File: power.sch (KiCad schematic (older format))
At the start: 8 parts

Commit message: Added some footprints. Basic board outline.
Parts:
- C1: renamed from C?; footprint (none) -> Capacitor_THT:CP_Radial_D5.0mm_P2.00mm; symbol Device:CP -> Device:C
- C2: renamed from C?; footprint (none) -> Capacitor_THT:C_Disc_D5.0mm_W2.5mm_P2.50mm
- F1: renamed from F?; footprint (none) -> Diode_THT:D_DO-15_P10.16mm_Horizontal
- J9: renamed from J?; footprint (none) -> Connector_USB:USB_B_OST_USB-B1HSxx_Horizontal
- R1: renamed from R?; footprint (none) -> Resistor_THT:R_Axial_DIN0411_L9.9mm_D3.6mm_P12.70mm_Horizontal
- SW1: renamed from SW?; footprint (none) -> Button_Switch_THT:SW_Push_1P2T_Vertical_E-Switch_800UDP8P1A1M6
- SW2: renamed from SW?; footprint (none) -> Button_Switch_THT:SW_PUSH-12mm
- gave numbers to parts that had none: 1
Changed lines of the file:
@@
 $Descr A4 11693 8268
 encoding utf-8
-Sheet 6 11
+Sheet 5 11
 Title "Neotron 32K"
 Date "2019-12-08"
@@
 ~RESET
 $Comp
-L Connector:USB_B J?
+L Connector:USB_B J9
 U 1 1 5DFCA02C
 P 3200 2400
-F 0 "J?" H 3200 2850 50  0000 C CNN
+F 0 "J9" H 3200 2850 50  0000 C CNN
 F 1 "USB_B" H 3200 2750 50  0000 C CNN
-F 2 "" H 3350 2350 50  0001 C CNN
+F 2 "Connector_USB:USB_B_OST_USB-B1HSxx_Horizontal" H 3350 2350 50  0001 C CNN
 F 3 " ~" H 3350 2350 50  0001 C CNN
 	1    3200 2400
@@
 $EndComp
 $Comp
-L power:+5V #PWR?
+L power:+5V #PWR011
 U 1 1 5DFCBF4D
 P 6300 2050
-F 0 "#PWR?" H 6300 1900 50  0001 C CNN
+F 0 "#PWR011" H 6300 1900 50  0001 C CNN
 F 1 "+5V" H 6315 2223 50  0000 C CNN
 F 2 "" H 6300 2050 50  0001 C CNN
@@
 NoConn ~ 3500 2500
 $Comp
-L Device:CP C?
+L Device:C C1
 U 1 1 5DFCD9F0
 P 5700 2300
-F 0 "C?" H 5818 2346 50  0000 L CNN
+F 0 "C1" H 5818 2346 50  0000 L CNN
 F 1 "47u" H 5818 2255 50  0000 L CNN
-F 2 "" H 5738 2150 50  0001 C CNN
+F 2 "Capacitor_THT:CP_Radial_D5.0mm_P2.00mm" H 5738 2150 50  0001 C CNN
 F 3 "~" H 5700 2300 50  0001 C CNN
 	1    5700 2300
@@
 $EndComp
 $Comp
-L Device:C C?
+L Device:C C2
 U 1 1 5DFCDDA8
 P 6100 2300
-F 0 "C?" H 6215 2346 50  0000 L CNN
+F 0 "C2" H 6215 2346 50  0000 L CNN
 F 1 "1u" H 6215 2255 50  0000 L CNN
-F 2 "" H 6138 2150 50  0001 C CNN
+F 2 "Capacitor_THT:C_Disc_D5.0mm_W2.5mm_P2.50mm" H 6138 2150 50  0001 C CNN
 F 3 "~" H 6100 2300 50  0001 C CNN
 	1    6100 2300
@@
 $EndComp
 $Comp
-L Device:Polyfuse F?
+L Device:Polyfuse F1
 U 1 1 5DFCE179
 P 4850 2100
-F 0 "F?" V 4625 2100 50  0000 C CNN
+F 0 "F1" V 4625 2100 50  0000 C CNN
 F 1 "250mA PTC" V 4716 2100 50  0000 C CNN
-F 2 "" H 4900 1900 50  0001 L CNN
+F 2 "Diode_THT:D_DO-15_P10.16mm_Horizontal" H 4900 1900 50  0001 L CNN
 F 3 "https://www.littelfuse.com/~/media/electronics/product_specifications/resettable_ptcs/littelfuse_ptc_rxef025_product_specification.pdf.pdf" H 4850 2100 50  0001 C CNN
 F 4 "RXEF025HF-ND" V 4850 2100 50  0001 C CNN "Digikey"
@@
 $EndComp
 $Comp
-L Device:D_TVS D?
+L Device:D_TVS D1
 U 1 1 5DFD0F1E
 P 5200 2300
-F 0 "D?" V 5154 2379 50  0000 L CNN
+F 0 "D1" V 5154 2379 50  0000 L CNN
 F 1 "SA5.0A" V 5245 2379 50  0000 L CNN
 F 2 "Diode_THT:D_DO-15_P12.70mm_Horizontal" H 5200 2300 50  0001 C CNN
@@
 Connection ~ 5700 2500
 $Comp
-L power:GND #PWR?
+L power:GND #PWR012
 U 1 1 5DFD4FCF
 P 6300 2550
-F 0 "#PWR?" H 6300 2300 50  0001 C CNN
+F 0 "#PWR012" H 6300 2300 50  0001 C CNN
 F 1 "GND" H 6305 2377 50  0000 C CNN
 F 2 "" H 6300 2550 50  0001 C CNN
@@
 Connection ~ 6100 2500
 $Comp
-L Switch:SW_Push SW?
+L Switch:SW_Push SW2
 U 1 1 5DFD5E14
 P 7400 2500
-F 0 "SW?" H 7400 2785 50  0000 C CNN
+F 0 "SW2" H 7400 2785 50  0000 C CNN
 F 1 "SW_Push" H 7400 2694 50  0000 C CNN
-F 2 "" H 7400 2700 50  0001 C CNN
+F 2 "Button_Switch_THT:SW_PUSH-12mm" H 7400 2700 50  0001 C CNN
 F 3 "~" H 7400 2700 50  0001 C CNN
 	1    7400 2500
@@
 $EndComp
 $Comp
-L Switch:SW_SPDT SW?
+L Switch:SW_SPDT SW1
 U 1 1 5DFD696E
 P 4000 2200
-F 0 "SW?" H 4000 2485 50  0000 C CNN
+F 0 "SW1" H 4000 2485 50  0000 C CNN
 F 1 "SW_SPDT" H 4000 2394 50  0000 C CNN
-F 2 "" H 4000 2200 50  0001 C CNN
+F 2 "Button_Switch_THT:SW_Push_1P2T_Vertical_E-Switch_800UDP8P1A1M6" H 4000 2200 50  0001 C CNN
 F 3 "~" H 4000 2200 50  0001 C CNN
 	1    4000 2200
@@
 	3200 2800 3200 2850
 $Comp
-L Device:R R?
+L Device:R R1
 U 1 1 5DFD98A8
 P 3100 3000
-F 0 "R?" H 3030 2954 50  0000 R CNN
+F 0 "R1" H 3030 2954 50  0000 R CNN
 F 1 "DNF" H 3030 3045 50  0000 R CNN
-F 2 "" V 3030 3000 50  0001 C CNN
+F 2 "Resistor_THT:R_Axial_DIN0411_L9.9mm_D3.6mm_P12.70mm_Horizontal" V 3030 3000 50  0001 C CNN
 F 3 "~" H 3100 3000 50  0001 C CNN
 	1    3100 3000
@@
 $EndComp
 $Comp
-L power:GND #PWR?
+L power:GND #PWR010
 U 1 1 5DFDADE6
 P 3100 3200
-F 0 "#PWR?" H 3100 2950 50  0001 C CNN
+F 0 "#PWR010" H 3100 2950 50  0001 C CNN
 F 1 "GND" H 3105 3027 50  0000 C CNN
 F 2 "" H 3100 3200 50  0001 C CNN
@@
 	4200 2100 4700 2100
 $Comp
-L power:GND #PWR?
+L power:GND #PWR013
 U 1 1 5DFDC03E
 P 7150 2600
-F 0 "#PWR?" H 7150 2350 50  0001 C CNN
+F 0 "#PWR013" H 7150 2350 50  0001 C CNN
 F 1 "GND" H 7155 2427 50  0000 C CNN
 F 2 "" H 7150 2600 50  0001 C CNN

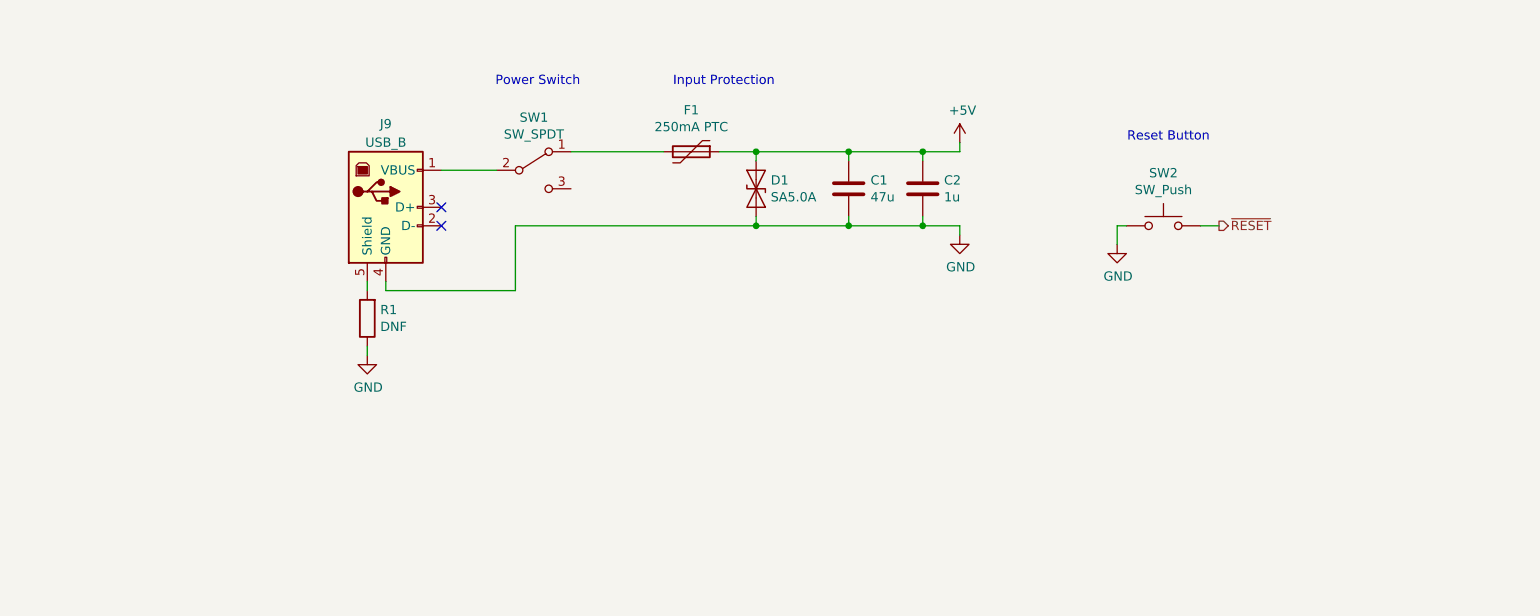
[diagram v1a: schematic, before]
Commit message: Completed Power, SD, MIDI, Parallel and Joystick sheets.
Switch to sheet based 100x part numbering.
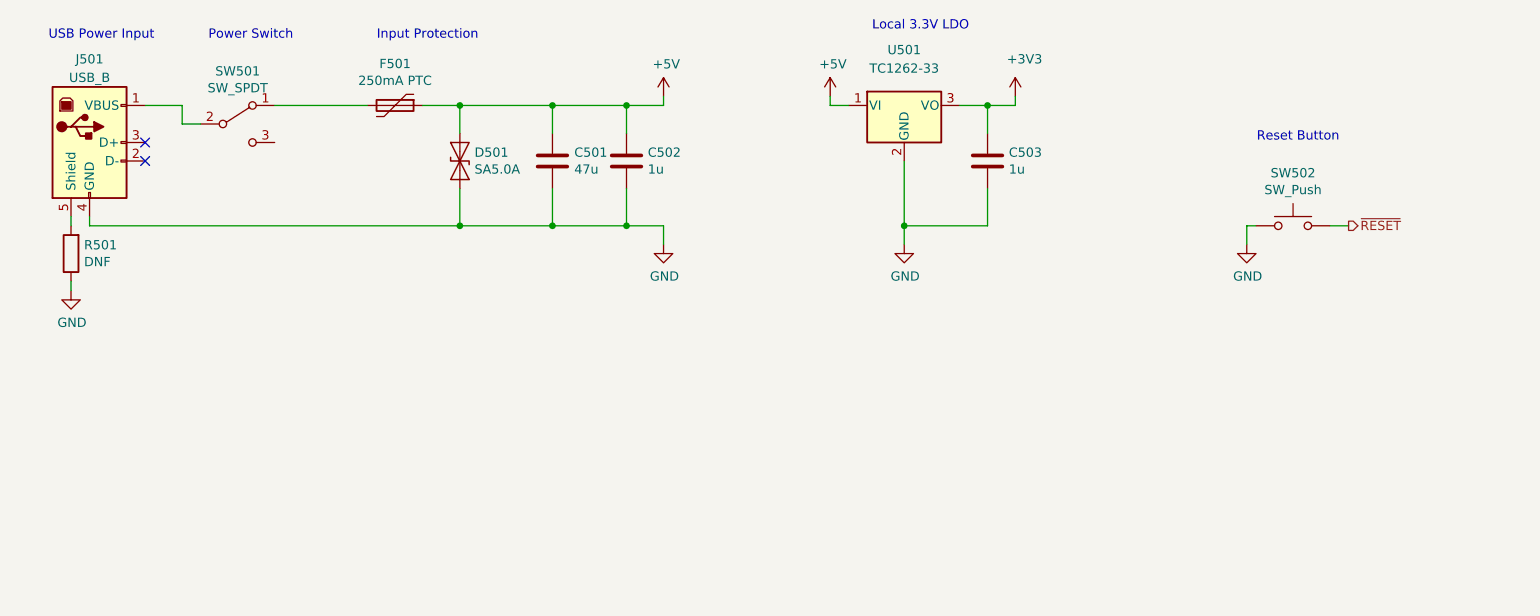
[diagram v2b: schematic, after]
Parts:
- added C503: 1u, Capacitor_THT:C_Disc_D5.0mm_W2.5mm_P2.50mm, symbol Device:C
- added U501: TC1262-33, symbol Regulator_Linear:TC1262-33
- renumbered C1 to C501, C2 to C502, D1 to D501, F1 to F501, J9 to J501, R1 to R501, SW1 to SW501, SW2 to SW502
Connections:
- net +5V: now also U501.1 (VI)
- net GND: now also C503.2, U501.2 (GND)
- new net +3V3: C503.1, U501.3 (VO)
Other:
- note added: "Local 3.3V LDO"
- note added: "USB Power Input"
- moved on the sheet: C501, C502, D501, F501, J501, R501, SW501, SW502

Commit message: Schematic capture draft complete.
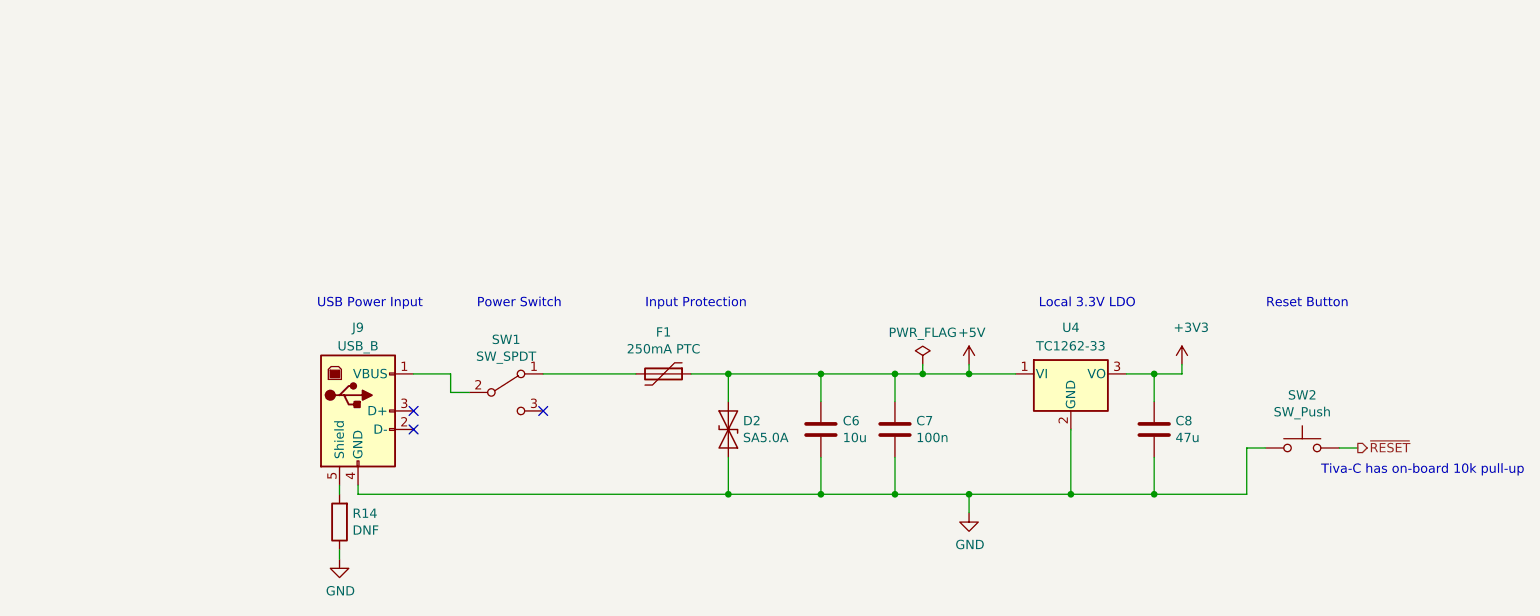
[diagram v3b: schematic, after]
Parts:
- C6: renamed from C501; value 47u -> 10u; footprint Capacitor_THT:CP_Radial_D5.0mm_P2.00mm -> Capacitor_THT:C_Disc_D3.0mm_W2.0mm_P2.50mm
- C7: renamed from C502; value 1u -> 100n; footprint Capacitor_THT:C_Disc_D5.0mm_W2.5mm_P2.50mm -> Capacitor_THT:C_Disc_D3.0mm_W2.0mm_P2.50mm
- C8: renamed from C503; value 1u -> 47u; footprint Capacitor_THT:C_Disc_D5.0mm_W2.5mm_P2.50mm -> Capacitor_THT:C_Disc_D3.0mm_W2.0mm_P2.50mm
- U4: renamed from U501; footprint (none) -> Package_TO_SOT_THT:TO-220-3_Vertical
- renumbered D501 to D2, F501 to F1, J501 to J9, R501 to R14, SW501 to SW1, SW502 to SW2
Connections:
- no-connect marks 2 -> 3
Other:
- note added: "Tiva-C has on-board 10k pull-up"
- moved on the sheet: C6, C7, C8, D2, F1, J9, R14, SW1, SW2, U4

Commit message: Work in progress.
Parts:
- removed SW1: SW_SPDT, Button_Switch_THT:SW_Push_1P2T_Vertical_E-Switch_800UDP8P1A1M6, symbol Switch:SW_SPDT
- added SW1: SW_SPST, Connector_PinHeader_2.54mm:PinHeader_1x02_P2.54mm_Vertical, symbol Switch:SW_SPST
- SW2: footprint Button_Switch_THT:SW_PUSH-12mm -> Connector_PinHeader_2.54mm:PinHeader_1x02_P2.54mm_Vertical
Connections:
- net at J9.1 (VBUS): now also SW1.1 (A)
- net at F1.2: now also SW1.2 (B)
- no-connect marks 3 -> 2
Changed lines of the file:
@@
 F 0 "SW2" H 8150 3985 50  0000 C CNN
 F 1 "SW_Push" H 8150 3894 50  0000 C CNN
-F 2 "Button_Switch_THT:SW_PUSH-12mm" H 8150 3900 50  0001 C CNN
+F 2 "Connector_PinHeader_2.54mm:PinHeader_1x02_P2.54mm_Vertical" H 8150 3900 50  0001 C CNN
 F 3 "~" H 8150 3900 50  0001 C CNN
 	1    8150 3700
-	1    0    0    -1
-$EndComp
-$Comp
-L Switch:SW_SPDT SW1
-U 1 1 5DFD696E
-P 3850 3400
-F 0 "SW1" H 3850 3685 50  0000 C CNN
-F 1 "SW_SPDT" H 3850 3594 50  0000 C CNN
-F 2 "Button_Switch_THT:SW_Push_1P2T_Vertical_E-Switch_800UDP8P1A1M6" H 3850 3400 50  0001 C CNN
-F 3 "~" H 3850 3400 50  0001 C CNN
-	1    3850 3400
 	1    0    0    -1
 $EndComp
@@
 Text Notes 3400 2950 2    50   ~ 0
 USB Power Input
-Wire Wire Line
-	3550 3300 3550 3400
-Wire Wire Line
-	3550 3400 3650 3400
 Wire Wire Line
 	6350 3950 6350 4050
@@
 Text Notes 9350 3850 2    50   ~ 0
 Tiva-C has on-board 10k pull-up
-NoConn ~ 4050 3500
 Wire Wire Line
 	5950 3300 6100 3300
@@
 Wire Wire Line
 	6100 3250 6100 3300
-Wire Wire Line
-	3350 3300 3550 3300
 Connection ~ 6100 3300
 Wire Wire Line
 	6100 3300 6350 3300
+$Comp
+L Switch:SW_SPST SW1
+U 1 1 5DFA9474
+P 3850 3300
+F 0 "SW1" H 3850 3535 50  0000 C CNN
+F 1 "SW_SPST" H 3850 3444 50  0000 C CNN
+F 2 "Connector_PinHeader_2.54mm:PinHeader_1x02_P2.54mm_Vertical" H 3850 3300 50  0001 C CNN
+F 3 "~" H 3850 3300 50  0001 C CNN
+	1    3850 3300
+	1    0    0    -1
+$EndComp
+Wire Wire Line
+	3350 3300 3650 3300
 $EndSCHEMATC

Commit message: Updated footprints: ) Swapped RS-232 DE9 for IDC header. ) Large caps are radial electrolytics. ) Made resistors a little smaller.
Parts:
- added R28: 330, Resistor_THT:R_Axial_DIN0207_L6.3mm_D2.5mm_P10.16mm_Horizontal, symbol Device:R
- C6, C8: footprint Capacitor_THT:C_Disc_D3.0mm_W2.0mm_P2.50mm -> Capacitor_THT:CP_Radial_D6.3mm_P2.50mm
- R14: footprint Resistor_THT:R_Axial_DIN0411_L9.9mm_D3.6mm_P12.70mm_Horizontal -> Resistor_THT:R_Axial_DIN0207_L6.3mm_D2.5mm_P10.16mm_Horizontal
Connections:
- net ~RESET: now also R28.1; no longer SW2.2
- new net: R28.2, SW2.2
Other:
- note added: "330R is for current limiting"
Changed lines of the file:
@@
 Comment4 ""
 $EndDescr
-Text HLabel 8450 3700 2    50   Output ~ 0
+Text HLabel 8850 3700 2    50   Output ~ 0
 ~RESET
 $Comp
@@
 F 0 "C6" H 5668 3646 50  0000 L CNN
 F 1 "10u" H 5668 3555 50  0000 L CNN
-F 2 "Capacitor_THT:C_Disc_D3.0mm_W2.0mm_P2.50mm" H 5588 3450 50  0001 C CNN
+F 2 "Capacitor_THT:CP_Radial_D6.3mm_P2.50mm" H 5588 3450 50  0001 C CNN
 F 3 "~" H 5550 3600 50  0001 C CNN
 	1    5550 3600
@@
 F 0 "R14" H 2880 4054 50  0000 R CNN
 F 1 "DNF" H 2880 4145 50  0000 R CNN
-F 2 "Resistor_THT:R_Axial_DIN0411_L9.9mm_D3.6mm_P12.70mm_Horizontal" V 2880 4100 50  0001 C CNN
+F 2 "Resistor_THT:R_Axial_DIN0207_L6.3mm_D2.5mm_P10.16mm_Horizontal" V 2880 4100 50  0001 C CNN
 F 3 "~" H 2950 4100 50  0001 C CNN
 	1    2950 4100
@@
 Wire Wire Line
 	8350 3700 8450 3700
-Text Notes 8400 2950 2    50   ~ 0
+Text Notes 8700 2950 2    50   ~ 0
 Reset Button
 Text Notes 5150 2950 2    50   ~ 0
@@
 F 0 "C8" H 7465 3646 50  0000 L CNN
 F 1 "47u" H 7465 3555 50  0000 L CNN
-F 2 "Capacitor_THT:C_Disc_D3.0mm_W2.0mm_P2.50mm" H 7388 3450 50  0001 C CNN
+F 2 "Capacitor_THT:CP_Radial_D6.3mm_P2.50mm" H 7388 3450 50  0001 C CNN
 F 3 "~" H 7350 3600 50  0001 C CNN
 	1    7350 3600
@@
 Wire Wire Line
 	3350 3300 3650 3300
+$Comp
+L Device:R R28
+U 1 1 5E09309F
+P 8600 3700
+F 0 "R28" V 8393 3700 50  0000 C CNN
+F 1 "330" V 8484 3700 50  0000 C CNN
+F 2 "Resistor_THT:R_Axial_DIN0207_L6.3mm_D2.5mm_P10.16mm_Horizontal" V 8530 3700 50  0001 C CNN
+F 3 "~" H 8600 3700 50  0001 C CNN
+	1    8600 3700
+	0    1    1    0
+$EndComp
+Wire Wire Line
+	8750 3700 8850 3700
+Text Notes 8000 3950 0    50   ~ 0
+330R is for current limiting
 $EndSCHEMATC

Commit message: Finished layout and silkscreen.
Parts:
- C6, C8: symbol Device:C -> Device:CP
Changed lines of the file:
@@
 Title "Neotron 32K Main PCB"
 Date "2019-12-16"
-Rev "0.6"
+Rev "XXREVISIONXX"
 Comp "github.com/neotron-compute/Neotron-32-Hardware"
 Comment1 "Copyright (c) Jonathan 'theJPster' Pallant"
@@
 $EndComp
 $Comp
-L power:+5V #PWR028
+L power:+5V #PWR?
 U 1 1 5DFCBF4D
 P 6350 3250
-F 0 "#PWR028" H 6350 3100 50  0001 C CNN
+F 0 "#PWR?" H 6350 3100 50  0001 C CNN
 F 1 "+5V" H 6365 3423 50  0000 C CNN
 F 2 "" H 6350 3250 50  0001 C CNN
@@
 NoConn ~ 3350 3600
 $Comp
-L Device:C C6
+L Device:CP C6
 U 1 1 5DFCD9F0
 P 5550 3600
@@
 	5050 3300 5550 3300
 $Comp
-L power:GND #PWR029
+L power:GND #PWR?
 U 1 1 5DFD4FCF
 P 6350 4050
-F 0 "#PWR029" H 6350 3800 50  0001 C CNN
+F 0 "#PWR?" H 6350 3800 50  0001 C CNN
 F 1 "GND" H 6355 3877 50  0000 C CNN
 F 2 "" H 6350 4050 50  0001 C CNN
@@
 $EndComp
 $Comp
-L power:GND #PWR027
+L power:GND #PWR?
 U 1 1 5DFDADE6
 P 2950 4300
-F 0 "#PWR027" H 2950 4050 50  0001 C CNN
+F 0 "#PWR?" H 2950 4050 50  0001 C CNN
 F 1 "GND" H 2955 4127 50  0000 C CNN
 F 2 "" H 2950 4300 50  0001 C CNN
@@
 $EndComp
 $Comp
-L Device:C C8
+L Device:CP C8
 U 1 1 5DF0ED61
 P 7350 3600
@@
 	7200 3300 7350 3300
 $Comp
-L power:+3V3 #PWR030
+L power:+3V3 #PWR?
 U 1 1 5DF1230F
 P 7500 3250
-F 0 "#PWR030" H 7500 3100 50  0001 C CNN
+F 0 "#PWR?" H 7500 3100 50  0001 C CNN
 F 1 "+3V3" H 7550 3450 50  0000 C CNN
 F 2 "" H 7500 3250 50  0001 C CNN
@@
 	5950 3300 6100 3300
 $Comp
-L power:PWR_FLAG #FLG01
+L power:PWR_FLAG #FLG?
 U 1 1 5E3AF755
 P 6100 3250
-F 0 "#FLG01" H 6100 3325 50  0001 C CNN
+F 0 "#FLG?" H 6100 3325 50  0001 C CNN
 F 1 "PWR_FLAG" H 6100 3423 50  0000 C CNN
 F 2 "" H 6100 3250 50  0001 C CNN
